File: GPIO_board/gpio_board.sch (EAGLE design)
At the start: 15 parts, among them J1 SWITCHES, J2 LED1, J3 LED2, Q1 IRF520, Q2 IRF520, Q3 IRF520, X1 PCI-E-164SLOT

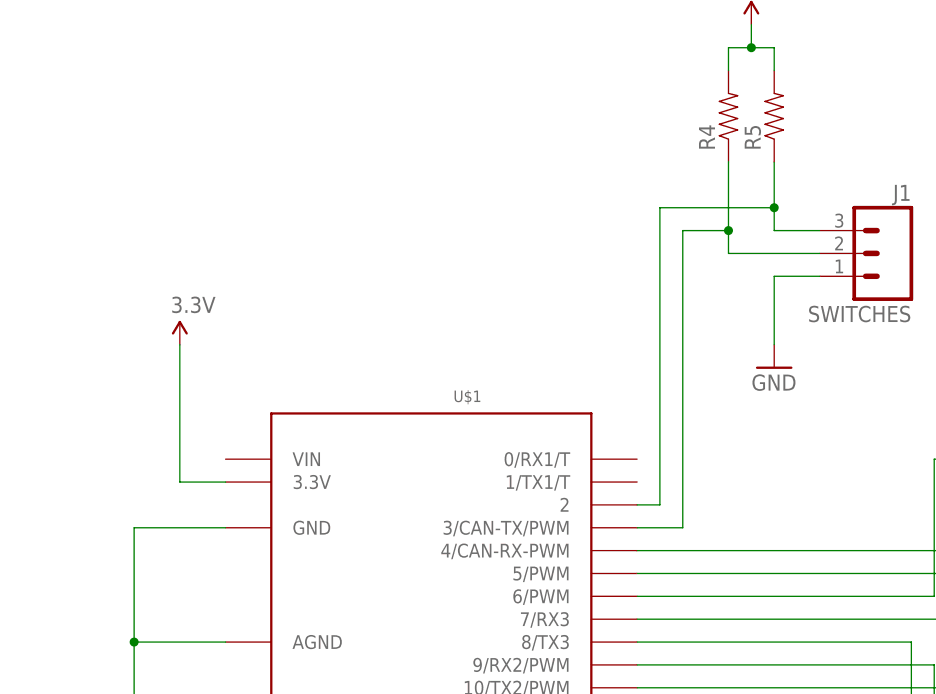
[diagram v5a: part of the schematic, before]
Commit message: added headers for VIN and serial port. fixed issues with redundant manual route to ground from pin 1 on teensy.
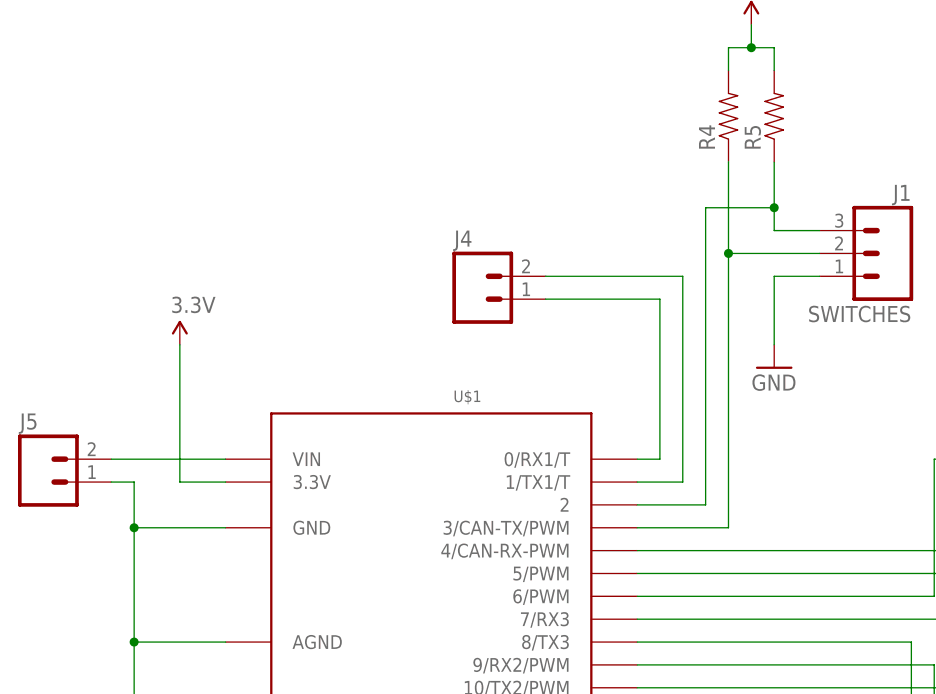
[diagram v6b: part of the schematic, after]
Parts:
- added J4, J5: (no value), SparkFun-Connectors:M02PTH
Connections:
- new net N$29: J4.1, U$1.0/RX1/T
- new net N$44: J4.2, U$1.1/TX1/T
- new net N$45: J5.2, U$1.VIN
- net GND: now also J5.1
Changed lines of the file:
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@@
 <part name="SUPPLY2" library="SparkFun-Aesthetics" deviceset="3.3V" device=""/>
 <part name="U$2" library="talon_lbr" deviceset="PROTO_GRID" device=""/>
+<part name="J4" library="SparkFun-Connectors" deviceset="M02" device="PTH"/>
+<part name="J5" library="SparkFun-Connectors" deviceset="M02" device="PTH"/>
 </parts>
 <sheets>
@@
 <instance part="SUPPLY2" gate="G$1" x="68.58" y="144.78"/>
 <instance part="U$2" gate="G$1" x="139.7" y="53.34" rot="R270"/>
+<instance part="J4" gate="G$1" x="101.6" y="149.86"/>
+<instance part="J5" gate="G$1" x="53.34" y="129.54"/>
 </instances>
 <busses>
 </busses>
 <nets>
-<net name="GND" class="1">
+<net name="GND" class="0">
 <segment>
 <pinref part="U$1" gate="G$1" pin="GND"/>
@@
 <wire x1="73.66" y1="111.76" x2="63.5" y2="111.76" width="0.1524" layer="91"/>
 <junction x="63.5" y="111.76"/>
+<pinref part="J5" gate="G$1" pin="1"/>
+<wire x1="60.96" y1="129.54" x2="63.5" y2="129.54" width="0.1524" layer="91"/>
+<wire x1="63.5" y1="129.54" x2="63.5" y2="124.46" width="0.1524" layer="91"/>
+<junction x="63.5" y="124.46"/>
 </segment>
 <segment>
@@
 <wire x1="134.62" y1="157.48" x2="134.62" y2="160.02" width="0.1524" layer="91"/>
 <wire x1="134.62" y1="160.02" x2="134.62" y2="165.1" width="0.1524" layer="91"/>
-<wire x1="121.92" y1="160.02" x2="134.62" y2="160.02" width="0.1524" layer="91"/>
+<wire x1="127" y1="160.02" x2="134.62" y2="160.02" width="0.1524" layer="91"/>
 <junction x="134.62" y="160.02"/>
 <pinref part="U$1" gate="G$1" pin="2"/>
-<wire x1="119.38" y1="127" x2="121.92" y2="127" width="0.1524" layer="91"/>
-<wire x1="121.92" y1="127" x2="121.92" y2="160.02" width="0.1524" layer="91"/>
+<wire x1="119.38" y1="127" x2="127" y2="127" width="0.1524" layer="91"/>
+<wire x1="127" y1="127" x2="127" y2="160.02" width="0.1524" layer="91"/>
 </segment>
 </net>
@@
 <segment>
 <pinref part="R4" gate="G$1" pin="1"/>
-<wire x1="129.54" y1="165.1" x2="129.54" y2="157.48" width="0.1524" layer="91"/>
+<wire x1="129.54" y1="165.1" x2="129.54" y2="154.94" width="0.1524" layer="91"/>
 <pinref part="J1" gate="J$1" pin="2"/>
-<wire x1="129.54" y1="157.48" x2="129.54" y2="154.94" width="0.1524" layer="91"/>
 <wire x1="129.54" y1="154.94" x2="139.7" y2="154.94" width="0.1524" layer="91"/>
-<wire x1="124.46" y1="124.46" x2="124.46" y2="157.48" width="0.1524" layer="91"/>
-<wire x1="124.46" y1="157.48" x2="129.54" y2="157.48" width="0.1524" layer="91"/>
-<junction x="129.54" y="157.48"/>
+<wire x1="129.54" y1="124.46" x2="129.54" y2="154.94" width="0.1524" layer="91"/>
+<junction x="129.54" y="154.94"/>
 <pinref part="U$1" gate="G$1" pin="3/CAN-TX/PWM"/>
-<wire x1="119.38" y1="124.46" x2="124.46" y2="124.46" width="0.1524" layer="91"/>
+<wire x1="119.38" y1="124.46" x2="129.54" y2="124.46" width="0.1524" layer="91"/>
 </segment>
 </net>
@@
 </segment>
 </net>
+<net name="N$29" class="0">
+<segment>
+<pinref part="U$1" gate="G$1" pin="0/RX1/T"/>
+<wire x1="119.38" y1="132.08" x2="121.92" y2="132.08" width="0.1524" layer="91"/>
+<wire x1="121.92" y1="132.08" x2="121.92" y2="149.86" width="0.1524" layer="91"/>
+<pinref part="J4" gate="G$1" pin="1"/>
+<wire x1="121.92" y1="149.86" x2="109.22" y2="149.86" width="0.1524" layer="91"/>
+</segment>
+</net>
+<net name="N$44" class="0">
+<segment>
+<pinref part="J4" gate="G$1" pin="2"/>
+<wire x1="109.22" y1="152.4" x2="124.46" y2="152.4" width="0.1524" layer="91"/>
+<wire x1="124.46" y1="152.4" x2="124.46" y2="129.54" width="0.1524" layer="91"/>
+<pinref part="U$1" gate="G$1" pin="1/TX1/T"/>
+<wire x1="124.46" y1="129.54" x2="119.38" y2="129.54" width="0.1524" layer="91"/>
+</segment>
+</net>
+<net name="N$45" class="0">
+<segment>
+<pinref part="J5" gate="G$1" pin="2"/>
+<pinref part="U$1" gate="G$1" pin="VIN"/>
+<wire x1="60.96" y1="132.08" x2="73.66" y2="132.08" width="0.1524" layer="91"/>
+</segment>
+</net>
